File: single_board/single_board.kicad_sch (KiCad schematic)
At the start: 113 parts, among them J1 CAN_OUT, J10 SPI Debug, J11 Screw_Terminal_01x02, J12 Conn_01x03, J13 Conn_01x04, J14 Screw_Terminal_01x02, J15 UART, J16 BOOTSEL, J17 Conn_01x03, J18 Conn_01x04, J19 Conn_01x03, J2 USB_C_Receptacle_USB2.0_16P, J20 Screw_Terminal_01x02, J21 Conn_01x04, J22 Conn_01x03, J23 Conn_01x04, J24 Screw_Terminal_01x02, J25 Conn_01x03, J26 Conn_01x04, J3 Conn_01x02, J4 Screw_Terminal_01x03, J5 490107670612, J6 Screw_Terminal_01x02, J7 Conn_01x03, J8 Conn_01x04, J9 SWD, Q1 AO3401A, Q2 2N7002, Q3 AO3401A, Q4 AO3401A, Q5 AO3401A, SW1 Button, U1 AP2112K-3.3, U2 TJA1042T-3, U3 USBLC6-2SC6, U4 LSM6DSV, U5 STM32G474VBTx, Y1 FC-135

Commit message: Layout pass 2
Rough placement of components and orientations
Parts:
- removed J4: Screw_Terminal_01x03, TerminalBlock:TerminalBlock_Xinya_XY308-2.54-3P_1x03_P2.54mm_Horizontal, symbol Connector:Screw_Terminal_01x03
- added J27, J28: Screw_Terminal_01x02, TerminalBlock:TerminalBlock_Xinya_XY308-2.54-2P_1x02_P2.54mm_Horizontal, symbol Connector:Screw_Terminal_01x02
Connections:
- net 5VIN: now also J27.2 (Pin_2)
- net FSR_SIG: now also U5.45 (PE14); no longer U5.44 (PE13)
- net GND: now also J27.1 (Pin_1), J28.1 (Pin_1)
- net v3v3IN: now also J28.2 (Pin_2)
- net FSR renamed FSR_ADC
- net FSR_ADC: now also U5.44 (PE13); no longer U5.45 (PE14)
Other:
- note added: "Analog, ADC3 3IN"
- note removed: "Analog, ADC4 1IN"
- moved on the sheet: C14, C15, C16, C17, C18, C19, C20, C21, C22, C23, C24, C25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

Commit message: IMU
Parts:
- added D5, D6: LED, LED_SMD:LED_0603_1608Metric_Pad1.05x0.95mm_HandSolder, symbol Device:LED
- added R29, R30: 10k, Resistor_SMD:R_0402_1005Metric_Pad0.72x0.64mm_HandSolder, symbol Device:R_Small
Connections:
- net GND: now also R29.2, R30.2
- new net: D6.1 (K), R30.1
- new net: D5.1 (K), R29.1
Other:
- note added: "Debug LEDs"
- note added: "For example: indicate encoder/motor direction; Verify or characterize that software, signal, and hardware all behave as expected"

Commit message: Layout pass 3
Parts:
- removed R2, R5, R8: 5.1k, Resistor_SMD:R_0603_1608Metric_Pad0.98x0.95mm_HandSolder, symbol Device:R_Small
- added R3, R7, R9: 1k, Capacitor_SMD:C_0402_1005Metric_Pad0.74x0.62mm_HandSolder, symbol Device:R_Small
- R18: renamed from R12; value 5.1k -> 1k; footprint Resistor_SMD:R_0603_1608Metric_Pad0.98x0.95mm_HandSolder -> Capacitor_SMD:C_0402_1005Metric_Pad0.74x0.62mm_HandSolder
- R21: renamed from R15; value 5.1k -> 1k; footprint Resistor_SMD:R_0603_1608Metric_Pad0.98x0.95mm_HandSolder -> Capacitor_SMD:C_0402_1005Metric_Pad0.74x0.62mm_HandSolder
- R24: renamed from R17; value 5.1k -> 1k; footprint Resistor_SMD:R_0603_1608Metric_Pad0.98x0.95mm_HandSolder -> Capacitor_SMD:C_0402_1005Metric_Pad0.74x0.62mm_HandSolder
- renumbered D7 to D2, D2 to D3, D5 to D4, D6 to D5, D3 to D6, D4 to D7, J9 to J10, J10 to J11, J11 to J12, J12 to J13, J13 to J14, J14 to J15, J15 to J16, J16 to J17, J17 to J18, J18 to J19, J19 to J20, J20 to J21, J21 to J22, J22 to J23, J23 to J24, J24 to J25, J25 to J26, J26 to J27, J27 to J3, J3 to J4, J28 to J5, J5 to J6, J6 to J7, J7 to J8, J8 to J9, Q3 to Q1, Q4 to Q2, Q5 to Q3, Q1 to Q4, Q2 to Q5, R7 to R1, R9 to R10, R29 to R11, R30 to R12, R28 to R13, R10 to R14, R11 to R15, R25 to R16, R26 to R17, R13 to R19, R20 to R2, R14 to R20, R16 to R22, R27 to R23, R18 to R25, R19 to R26, R21 to R27, R22 to R28, R23 to R29, R24 to R30, R1 to R4, R3 to R5, R4 to R6, R6 to R8
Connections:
- net 5V: no longer D3.3 (A)
- net HEARTBEAT: now also U5.58 (PD11); no longer U5.30 (PC4)
- net TRI_LED_B: now also U5.94 (PB7), R9.2; no longer U5.93 (PB6)
- net TRI_LED_G: now also U5.92 (PB5), R7.2; no longer U5.94 (PB7)
- net TRI_LED_R: now also U5.93 (PB6), R3.2; no longer U5.92 (PB5)
- net v3v3: now also D3.3 (A)
- net LED2: now reaches D5.2 (A)
- net LED2: now also U5.31 (PC5)
- net at D3.2 (BK): now also R9.1
- net at D3.1 (RK): now also R3.1
- net at D3.4 (GK): now also R7.1
- net LED1: now reaches D4.2 (A)
- net LED1: now also U5.30 (PC4)
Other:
- moved on the sheet: D1, D2, D3, D4, D5, R1, R11, R12, R2

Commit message: Signal Traces
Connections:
- net CAN_LED: now also U5.54 (PB15); no longer U5.50 (PB11)
- net HEARTBEAT: now also U5.55 (PD8); no longer U5.58 (PD11)
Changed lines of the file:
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@@
 	)
 	(label "CAN_LED"
-		(at 260.35 195.58 0)
+		(at 260.35 205.74 0)
 		(effects
 			(font
@@
 	)
 	(label "HEARTBEAT"
-		(at 214.63 220.98 180)
-		(effects
-			(font
+		(at 214.63 213.36 180)
+		(effects
+			(font

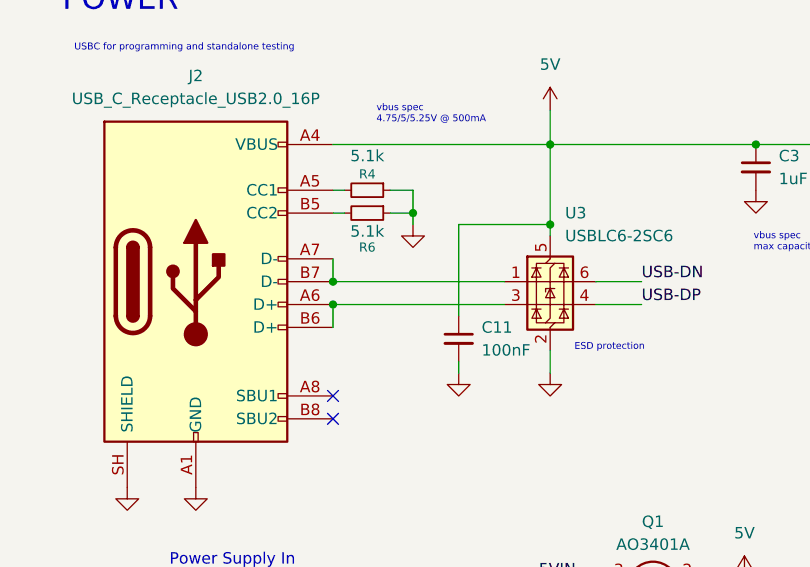
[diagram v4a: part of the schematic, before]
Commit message: Diff pairs, layer 1 power
Net classes and rules
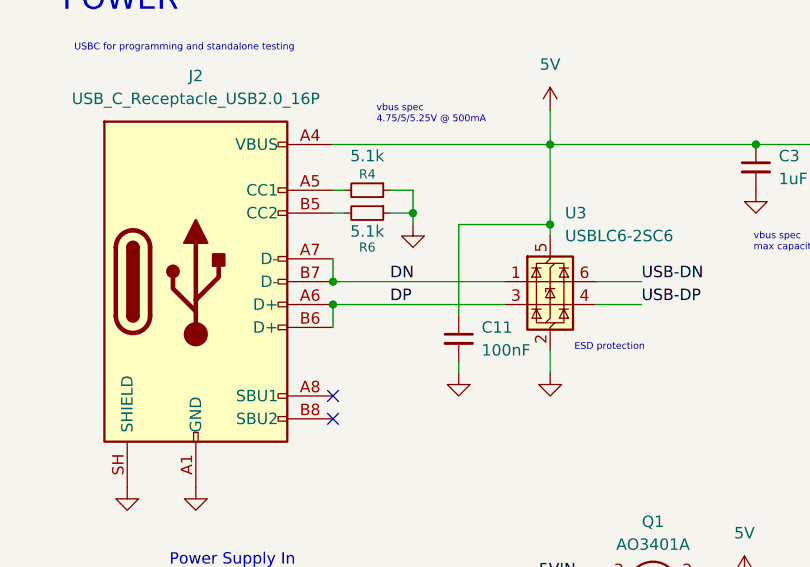
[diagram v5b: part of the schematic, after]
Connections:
- net DP: now reaches J2.A6 (D+), J2.B6 (D+), U3.3 (I/O2)
- net DN: now reaches J2.A7 (D-), J2.B7 (D-), U3.1 (I/O1)
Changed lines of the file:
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@@
+		)
+	)
+	(label "DP"
+		(at 49.53 50.8 0)
+		(effects
+			(font
+				(size 1.27 1.27)
+			)
+			(justify left bottom)
 		)
 	)
@@
 		(effects
 			(font
+				(size 1.27 1.27)
+			)
+			(justify left bottom)
+		)
+	)
+	(label "DN"
+		(at 49.53 48.26 0)
+		(effects
+			(font

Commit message: 80x80
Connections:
- net v3v3IN: no longer J10.1 (Pin_1), J6.6, Q3.3 (D)
- new net v3v3IN_debug: J10.1 (Pin_1), J6.6, Q3.3 (D)
- no-connect marks 6 -> 36
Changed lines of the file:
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@@
 	)
 	(no_connect
+		(at 214.63 142.24)
+	)
+	(no_connect
+		(at 260.35 147.32)
+	)
+	(no_connect
+		(at 214.63 180.34)
+	)
+	(no_connect
+		(at 214.63 134.62)
+	)
+	(no_connect
+		(at 260.35 129.54)
+	)
+	(no_connect
+		(at 260.35 149.86)
+	)
+	(no_connect
+		(at 214.63 198.12)
+	)
+	(no_connect
 		(at 43.18 60.96)
 	)
 	(no_connect
+		(at 214.63 220.98)
+	)
+	(no_connect
+		(at 214.63 208.28)
+	)
+	(no_connect
 		(at 229.87 114.3)
 	)
@@
 	)
 	(no_connect
+		(at 260.35 167.64)
+	)
+	(no_connect
+		(at 214.63 167.64)
+	)
+	(no_connect
+		(at 214.63 137.16)
+	)
+	(no_connect
+		(at 214.63 144.78)
+	)
+	(no_connect
+		(at 260.35 243.84)
+	)
+	(no_connect
+		(at 214.63 139.7)
+	)
+	(no_connect
+		(at 260.35 190.5)
+	)
+	(no_connect
+		(at 214.63 160.02)
+	)
+	(no_connect
+		(at 214.63 218.44)
+	)
+	(no_connect
+		(at 260.35 162.56)
+	)
+	(no_connect
+		(at 260.35 172.72)
+	)
+	(no_connect
+		(at 260.35 170.18)
+	)
+	(no_connect
+		(at 214.63 215.9)
+	)
+	(no_connect
+		(at 260.35 137.16)
+	)
+	(no_connect
 		(at 363.22 129.54)
 	)
@@
 		(at 363.22 133.35)
 	)
+	(no_connect
+		(at 260.35 195.58)
+	)
+	(no_connect
+		(at 260.35 144.78)
+	)
+	(no_connect
+		(at 260.35 193.04)
+	)
+	(no_connect
+		(at 214.63 177.8)
+	)
+	(no_connect
+		(at 214.63 205.74)
+	)
+	(no_connect
+		(at 214.63 195.58)
+	)
+	(no_connect
+		(at 214.63 193.04)
+	)
 	(wire
 		(pts
@@
 	(wire
 		(pts
-			(xy 327.66 152.4) (xy 335.28 152.4)
+			(xy 321.31 152.4) (xy 335.28 152.4)
 		)
 		(stroke
@@
 		)
 	)
+	(label "v3v3IN_debug"
+		(at 321.31 152.4 0)
+		(effects
+			(font
+				(size 1.27 1.27)
+			)
+			(justify left bottom)
+		)
+	)
 	(label "v3v3IN"
 		(at 66.04 107.95 0)
@@
 		)
 	)
-	(label "v3v3IN"
-		(at 311.15 156.21 180)
-		(effects
-			(font
-				(size 1.27 1.27)
-			)
-			(justify right bottom)
-		)
-	)
 	(label "INT1"
 		(at 396.24 129.54 0)
@@
 		)
 	)
-	(label "v3v3IN"
+	(label "v3v3IN_debug"
 		(at 323.85 130.81 0)
 		(effects
@@
 		)
 	)
+	(label "v3v3IN_debug"
+		(at 311.15 156.21 180)
+		(effects
+			(font
+				(size 1.27 1.27)
+			)
+			(justify right bottom)
+		)
+	)
 	(label "ENC2_B"
 		(at 27.94 172.72 0)
@@
 		(effects
 			(font
-				(size 1.27 1.27)
-			)
-			(justify left bottom)
-		)
-	)
-	(label "v3v3IN"
-		(at 327.66 152.4 0)
-		(effects
-			(font

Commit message: Update Schematic
New footprints
Clean up schematic
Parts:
- removed C1, C9: 1uF, Capacitor_SMD:C_0402_1005Metric_Pad0.74x0.62mm_HandSolder, symbol Device:C_Small
- removed C10, C2: 100nF, Capacitor_SMD:C_0402_1005Metric_Pad0.74x0.62mm_HandSolder, symbol Device:C_Small
- removed C8: 10nF, Capacitor_SMD:C_0402_1005Metric_Pad0.74x0.62mm_HandSolder, symbol Device:C_Small
- removed J10: SWD, Connector_PinHeader_2.54mm:PinHeader_1x05_P2.54mm_Vertical, symbol Connector_Generic:Conn_01x05
- removed J12, J15, J21, J25, J3, J5, J7: Screw_Terminal_01x02, TerminalBlock:TerminalBlock_Xinya_XY308-2.54-2P_1x02_P2.54mm_Horizontal, symbol Connector:Screw_Terminal_01x02
- removed J13, J18, J20, J23, J26, J8: Conn_01x03, Connector_PinHeader_2.54mm:PinHeader_1x03_P2.54mm_Vertical, symbol Connector_Generic:Conn_01x03
- removed J14, J19, J22, J24, J27, J9: Conn_01x04, Connector_PinHeader_2.54mm:PinHeader_1x04_P2.54mm_Vertical, symbol Connector_Generic:Conn_01x04
- removed J16: UART, Connector_PinHeader_2.54mm:PinHeader_1x03_P2.54mm_Vertical, symbol Connector_Generic:Conn_01x03
- removed J6: 490107670612, Rover:490107670612, symbol Connector:TC2030
- removed R10, R5: 60, Resistor_SMD:R_0402_1005Metric_Pad0.72x0.64mm_HandSolder, symbol Device:R_Small
- removed R13: 10k, Resistor_SMD:R_0402_1005Metric_Pad0.72x0.64mm_HandSolder, symbol Device:R_Small
- removed R8: 120, Resistor_SMD:R_0402_1005Metric_Pad0.72x0.64mm_HandSolder, symbol Device:R_Small
- removed U2: TJA1042T-3, Package_SO:SOIC-8_3.9x4.9mm_P1.27mm, symbol Interface_CAN_LIN:TJA1042T-3
- added C37, C39: 1uF, Capacitor_SMD:C_0402_1005Metric, symbol Device:C_Small
- added C38, C40: 100nF, Capacitor_SMD:C_0402_1005Metric, symbol Device:C_Small
- added C41: 10nF, Capacitor_SMD:C_0402_1005Metric, symbol Device:C_Small
- added J3: RST, Connector_PinHeader_2.54mm:PinHeader_1x01_P2.54mm_Vertical, symbol Connector_Generic:Conn_01x01
- added J30, J31, J33, J35, J36, J37: JST_GH_H, Connector_JST:JST_GH_SM02B-GHS-TB_1x02-1MP_P1.25mm_Horizontal, symbol Connector_Generic_MountingPin:Conn_01x02_MountingPin
- added J32, J34, J38, J39, J40, J41, J42, J43, J44, J45, J46, J47, J48, J49, J50: PB_Vertical, Connector_Molex:Molex_PicoBlade_53047-0410_1x04_P1.25mm_Vertical, symbol Connector_Generic:Conn_01x04
- added R31: 10k, Resistor_SMD:R_0402_1005Metric, symbol Device:R_Small
- added R32: 120, Resistor_SMD:R_0402_1005Metric, symbol Device:R_Small
- added R33, R34: 60, Resistor_SMD:R_0402_1005Metric, symbol Device:R_Small
- added U6: (no value), Package_SO:SOIC-8_3.9x4.9mm_P1.27mm, symbol Rover:TJA1042
- C11, C12, C13, C14, C15, C16, C17, C18, C19, C20, C21, C22, C23, C24, C25, C26, C27, C28, C29, C3, C30, C31, C32, C33, C34, C35, C36, C4, C5, C6, C7: footprint Capacitor_SMD:C_0402_1005Metric_Pad0.74x0.62mm_HandSolder -> Capacitor_SMD:C_0402_1005Metric
- D1, D2, D4, D5, D6, D7: footprint LED_SMD:LED_0603_1608Metric_Pad1.05x0.95mm_HandSolder -> Diode_SMD:D_0603_1608Metric
- H1, H2, H3, H4: footprint MountingHole:MountingHole_2.5mm_Pad -> MountingHole:MountingHole_5.3mm_M5_Pad
- J1: value CAN_OUT -> SWD
- R1, R11, R12, R14, R15, R16, R17, R19, R2, R20, R22, R23, R25, R26, R27, R28, R29, R30: footprint Resistor_SMD:R_0402_1005Metric_Pad0.72x0.64mm_HandSolder -> Resistor_SMD:R_0402_1005Metric
- R18, R21, R24, R3, R7, R9: footprint Capacitor_SMD:C_0402_1005Metric_Pad0.74x0.62mm_HandSolder -> Resistor_SMD:R_0402_1005Metric
- R4, R6: footprint Resistor_SMD:R_0603_1608Metric_Pad0.98x0.95mm_HandSolder -> Resistor_SMD:R_0603_1608Metric
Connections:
- net can_DN is gone; now on net SWDIO: J1.3 (Pin_3)
- net can_DP is gone; now on net GND: J1.2 (Pin_2)
- net 5V: now also C37.1, C38.1, J39.3 (Pin_3), J40.3 (Pin_3), J41.3 (Pin_3), J42.3 (Pin_3), J43.3 (Pin_3), J44.3 (Pin_3), U6.3 (VCC)
- net 5VIN: now also J34.1 (Pin_1)
- net CAN_STB: now also R31.1, U6.8 (STB)
- net DIR1: now also J38.1 (Pin_1)
- net DIR2: now also J45.1 (Pin_1)
- net DIR3: now also J46.1 (Pin_1)
- net DIR4: now also J47.1 (Pin_1)
- net DIR5: now also J48.1 (Pin_1)
- net DIR6: now also J49.1 (Pin_1)
- net ENC1_A: now also J39.1 (Pin_1)
- net ENC1_B: now also J39.2 (Pin_2)
- net ENC2_A: now also J40.1 (Pin_1)
- net ENC2_B: now also J40.2 (Pin_2)
- net ENC3_A: now also J41.1 (Pin_1)
- net ENC3_B: now also J41.2 (Pin_2)
- net ENC4_A: now also J42.1 (Pin_1)
- net ENC4_B: now also J42.2 (Pin_2)
- net ENC5_A: now also J43.1 (Pin_1)
- net ENC5_B: now also J43.2 (Pin_2)
- net ENC6_A: now also J44.1 (Pin_1)
- net ENC6_B: now also J44.2 (Pin_2)
- net FSR_ADC: now also J30.2 (Pin_2)
- net GND: now also C37.2, C38.2, C39.2, C40.2, C41.2, J30.MP (MountPin), J31.2 (Pin_2), J31.MP (MountPin), J32.3 (Pin_3), J33.2 (Pin_2), J33.MP (MountPin), J34.2 (Pin_2), J34.4 (Pin_4), J35.MP (MountPin), J36.2 (Pin_2), J36.MP (MountPin), J37.MP (MountPin), J38.3 (Pin_3), J39.4 (Pin_4), J40.4 (Pin_4), J41.4 (Pin_4), J42.4 (Pin_4), J43.4 (Pin_4), J44.4 (Pin_4), J45.3 (Pin_3), J46.3 (Pin_3), J47.3 (Pin_3), J48.3 (Pin_3), J49.3 (Pin_3), J50.3 (Pin_3), R31.2, U6.2 (GND); no longer J1.1 (Pin_1), J1.4 (Pin_4)
- net IMU_MOSI: now also U5.92 (PB5); no longer U5.81 (PC12)
- net INT1: now also U5.93 (PB6); no longer U5.85 (PD3)
- net INT2: now also U5.88 (PD6); no longer U5.86 (PD4)
- net LimitSwitch1: now also J31.1 (Pin_1)
- net LimitSwitch2: now also J36.1 (Pin_1)
- net LimitSwitch3: now also J33.1 (Pin_1)
- net PWM1: now also J38.2 (Pin_2)
- net PWM2: now also J45.2 (Pin_2)
- net PWM3: now also J46.2 (Pin_2)
- net PWM4: now also J47.2 (Pin_2)
- net PWM5: now also J48.2 (Pin_2)
- net PWM6: now also J49.2 (Pin_2)
- net RST: now also J3.1 (Pin_1)
- net SWCLK: now also J1.4 (Pin_4)
- net TRI_LED_B: now also U5.87 (PD5); no longer U5.94 (PB7)
- net TRI_LED_G: now also U5.85 (PD3); no longer U5.92 (PB5)
- net TRI_LED_R: now also U5.86 (PD4); no longer U5.93 (PB6)
- net UART4_RX: now also J32.1 (Pin_1)
- net UART4_TX: now also J32.2 (Pin_2)
- net v3v3: now also C39.1, C40.1, J37.1 (Pin_1), U6.5 (VIO)
- net v3v3IN: now also J34.3 (Pin_3)
- net v3v3IN_debug: now also J1.1 (Pin_1)
- net at Q4.3 (D): now also J30.1 (Pin_1)
- net at Q5.3 (D): now also J37.2 (Pin_2)
- net L_SW2: now reaches U5.42 (PE11)
- net L_SW2: now also R22.2
- net L_SW3: now reaches U5.43 (PE12)
- net L_SW3: now also R25.2
- net UART5_RX: now reaches U5.84 (PD2)
- net UART5_RX: now also J50.1 (Pin_1)
- net FDCAN_RX renamed CAN_RX
- net CAN_RX: now also U6.4 (RXD)
- net FDCAN_TX renamed CAN_TX
- net CAN_TX: now also U6.1 (TXD)
- net LS1: no longer names the net of U5.39 (PE8)
- net LS1: no longer R20.2
- net LS2: no longer names the net of U5.40 (PE9)
- net LS2: no longer R22.2
- net LS3 renamed L_SW1
- net L_SW1: now also R20.2; no longer R25.2
- new net: C41.1, R33.2, R34.1
- new net CAN_DN: J35.2 (Pin_2), R32.2, R34.2, U6.6 (CANL)
- new net CAN_DP: J35.1 (Pin_1), R32.1, R33.1, U6.7 (CANH)
- new net UART5_TX: J50.2 (Pin_2), U5.81 (PC12)
- no-connect marks 36 -> 41
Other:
- note added: "AN5093 p32 reference design vbat complicates routing, leave floating"
- note added: "Communication Interface"
- note added: "Encoders for DC Motors: Pin Arrangement for absolute encoder (ENC_B to PWM input) Optional ENC_A for quadrature"
- note added: "Encoders for Stepper Motors: Pin Arrangement for quadrature encoder Deactivate ENC1_A for absolute"
- note added: "Force Sensor"
- note added: "Laser Diode"
- note added: "Limit Switches"
- note added: "Perception Interface / debug"
- note added: "Reverse input protection fets"
- note added: "STLINK 5V"
- note added: "weaker 1k pullup to compensate for extra wire length 120ohm resistor to dampen any reflections"
- note removed: "DC Motors Pin Arrangement for absolute encoder (ENC_B to PWM input) Optional ENC_A for quadrature"
- note removed: "Limit Switches, Laser, Force Sensor"
- note removed: "Perception interface"
- note removed: "Stepper Motors Pin Arrangement for quadrature encoder"
- note removed: "Use only PWM read channel for absolute; Pin type from Encoder Mode to PWM Input on CHx."
- moved on the sheet: C11, C14, C15, C16, C17, C18, C19, C20, C21, C22, C23, C24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

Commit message: I2C, connectors
Update connectors, add I2C bus to MCU
TODO: routing new connectors
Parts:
- removed J50: PB_Vertical, Connector_Molex:Molex_PicoBlade_53047-0410_1x04_P1.25mm_Vertical, symbol Connector_Generic:Conn_01x04
- added J5: Conn_01x02, Connector_Coaxial:MMCX_Molex_73415-0961_Horizontal_0.8mm-PCB, symbol Connector_Generic:Conn_01x02
- added J51: JST_GH_H, Connector_JST:JST_GH_SM02B-GHS-TB_1x02-1MP_P1.25mm_Horizontal, symbol Connector_Generic_MountingPin:Conn_01x02_MountingPin
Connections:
- net GND: now also J51.MP (MountPin)
- net UART5_RX: now also J5.1 (Pin_1)
- net UART5_TX: now also J5.2 (Pin_2)
- net I2C_SDA: now reaches U5.69 (PA8)
- net I2C_SDA: now also J51.1 (Pin_1)
- net I2C_SCL: now reaches U5.70 (PA9)
- net I2C_SCL: now also J51.2 (Pin_2)
- no-connect marks 41 -> 38
